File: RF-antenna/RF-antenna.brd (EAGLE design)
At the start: 108.2 x 108.2 mm, 48 parts, among them CON1 UMC_CONNECTORREGULAR, CON2 UMC_CONNECTORREGULAR, CON3 UMC_CONNECTORREGULAR, CON4 UMC_CONNECTORREGULAR, CON5 UMC_CONNECTORREGULAR, CON6 UMC_CONNECTORREGULAR, U1 THS3091DDAR, U2 THS3091DDAR, U3 THS3091DDAR

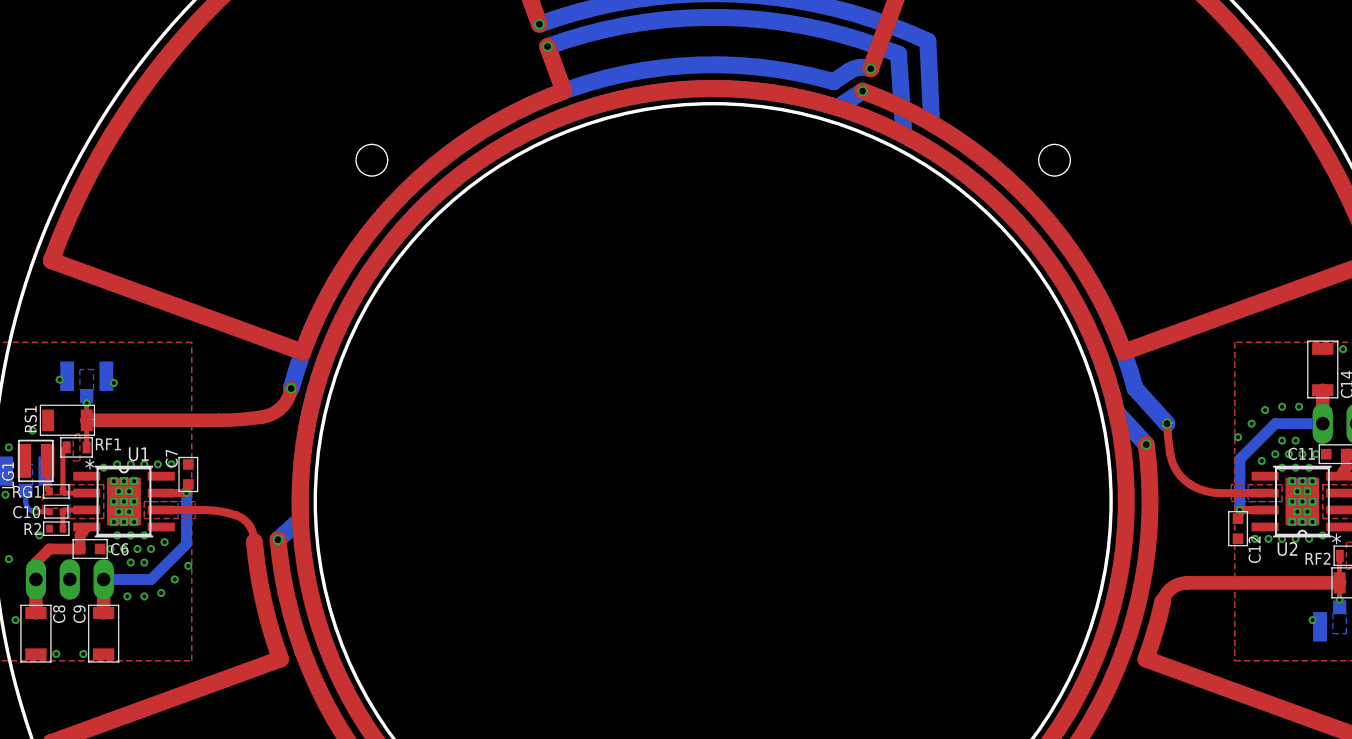
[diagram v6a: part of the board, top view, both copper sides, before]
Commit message: Fix antenna polarity
The polarity of half of each of the D-shaped antennas was incorrect. I've adjusted so that the D antennas produce B fields pointing along the diagonal as desired.

DSB
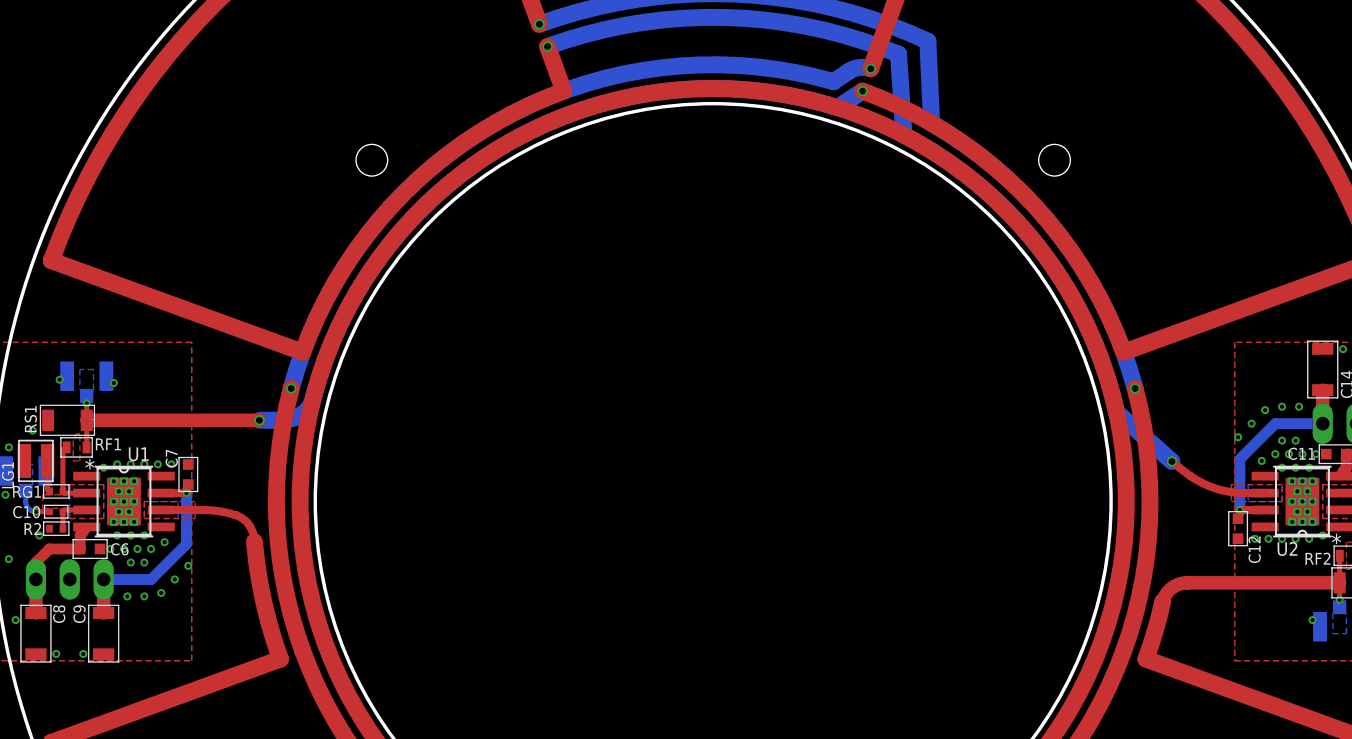
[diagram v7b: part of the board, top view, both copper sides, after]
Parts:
- moved LW5 8.95 mm to (95.5, 54.8)
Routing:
- net D1_COIL: track 372.8 -> 377.4 mm
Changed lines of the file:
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@@
 <element name="LW3" library="RFantenna" package="LITZ_100MHZ" value="LITZ_TERM" x="19.685" y="51.1048"/>
 <element name="LW4" library="RFantenna" package="LITZ_100MHZ" value="LITZ_TERM" x="7.112" y="60.198"/>
-<element name="LW5" library="RFantenna" package="LITZ_100MHZ" value="LITZ_TERM" x="88.138" y="59.944"/>
+<element name="LW5" library="RFantenna" package="LITZ_100MHZ" value="LITZ_TERM" x="95.4532" y="54.7878"/>
 <element name="LW6" library="RFantenna" package="LITZ_100MHZ" value="LITZ_TERM" x="101.092" y="48.006"/>
 </elements>
@@
 <wire x1="53.34" y1="21.9456" x2="52.324" y2="23.114" width="1.016" layer="1" curve="72.387043"/>
 <wire x1="55.88" y1="23.114" x2="55.858796875" y2="23.1638375" width="0" layer="19" extent="1-1"/>
-<wire x1="52.324" y1="23.114" x2="52.345203125" y2="23.1638375" width="0" layer="19" extent="1-1"/>
+<wire x1="52.345203125" y1="23.1638375" x2="52.324" y2="23.114" width="0" layer="19" extent="1-1"/>
 </signal>
 <signal name="D1_COIL">
@@
 <wire x1="4.456159375" y1="36.032390625" x2="21.641259375" y2="42.28725625" width="1.27" layer="1"/>
 <wire x1="21.641259375" y1="42.28725625" x2="19.689453125" y2="51.091290625" width="1.27" layer="1" curve="-14.999998"/>
-<wire x1="23.31203125" y1="42.89536875" x2="21.460684375" y2="51.24625625" width="1.27" layer="1" curve="-15.000001"/>
 <wire x1="103.747840625" y1="72.171609375" x2="72.171609375" y2="103.747840625" width="1.27" layer="1" curve="49.999998"/>
 <wire x1="84.89196875" y1="65.30863125" x2="65.30863125" y2="84.89196875" width="1.27" layer="1" curve="50.000003"/>
 <wire x1="84.89196875" y1="65.30863125" x2="103.747840625" y2="72.171609375" width="1.27" layer="1"/>
-<via x="21.460684375" y="51.24625625" extent="1-16" drill="0.508"/>
 <via x="65.30863125" y="84.89196875" extent="1-16" drill="0.508"/>
 <wire x1="72.171609375" y1="103.747840625" x2="65.91674375" y2="86.562740625" width="1.27" layer="1"/>
 <wire x1="63.133534375" y1="85.5987" x2="22.452475" y2="62.582465625" width="1.27" layer="16" curve="91"/>
-<wire x1="63.420271875" y1="83.65578125" x2="23.14349375" y2="52.750321875" width="1.27" layer="16" curve="110.000002"/>
 <wire x1="63.420271875" y1="83.65578125" x2="65.30863125" y2="84.89196875" width="1.27" layer="16"/>
 <wire x1="63.133534375" y1="85.5987" x2="64.262" y2="86.36" width="1.27" layer="16"/>
 <wire x1="64.262" y1="86.36" x2="65.91674375" y2="86.562740625" width="1.27" layer="16" curve="-54.03957"/>
 <via x="65.91674375" y="86.562740625" extent="1-16" drill="0.508"/>
-<wire x1="23.14349375" y1="52.750321875" x2="21.460684375" y2="51.24625625" width="1.27" layer="16"/>
 <wire x1="12.7" y1="53.467" x2="15.8496" y2="53.467" width="0.6096" layer="1"/>
 <wire x1="15.8496" y1="53.467" x2="18.288" y2="53.086" width="0.6096" layer="1" curve="-17.761316"/>
@@
 <wire x1="19.304" y1="52.324" x2="19.685" y2="51.1048" width="0.6096" layer="1" curve="-33.335057"/>
 <via x="22.452475" y="62.582465625" extent="1-16" drill="0.508"/>
-<wire x1="7.1142" y1="60.198" x2="17.018" y2="60.198" width="1.016" layer="1"/>
-<wire x1="17.018" y1="60.198" x2="20.32" y2="60.452" width="1.016" layer="1" curve="8.797411"/>
-<wire x1="20.32" y1="60.452" x2="22.452475" y2="62.582465625" width="1.016" layer="1" curve="72.351251"/>
+<wire x1="23.31203125" y1="42.89536875" x2="22.452475" y2="62.582465625" width="1.27" layer="1" curve="-35"/>
+<wire x1="63.420271875" y1="83.65578125" x2="24.169890625" y2="62.122284375" width="1.27" layer="16" curve="92.500001"/>
+<wire x1="24.169890625" y1="62.122284375" x2="24.0538" y2="61.6458" width="1.27" layer="16"/>
+<wire x1="24.0538" y1="61.6458" x2="22.9108" y2="60.452" width="1.27" layer="16" curve="-44.249514"/>
+<wire x1="22.9108" y1="60.452" x2="21.1582" y2="60.198" width="1.27" layer="16" curve="-24.404178"/>
+<wire x1="21.1582" y1="60.198" x2="20.066" y2="60.198" width="1.27" layer="16"/>
+<via x="20.066" y="60.198" extent="1-16" drill="0.508"/>
+<wire x1="7.1142" y1="60.198" x2="20.066" y2="60.198" width="1.016" layer="1"/>
 <wire x1="19.689453125" y1="51.091290625" x2="19.685" y2="51.1048" width="0" layer="19" extent="1-1"/>
 <wire x1="7.112" y1="60.198" x2="7.112" y2="60.2002" width="0" layer="19" extent="1-1"/>
@@
 <wire x1="103.747840625" y1="36.032390625" x2="86.562740625" y2="42.28725625" width="1.27" layer="1"/>
 <wire x1="86.562740625" y1="42.28725625" x2="87.82716875" y2="46.625309375" width="1.27" layer="1" curve="7.499999"/>
-<wire x1="84.89196875" y1="42.89536875" x2="86.58768125" y2="58.378821875" width="1.27" layer="1" curve="27.5"/>
 <wire x1="68.410665625" y1="81.588690625" x2="84.355459375" y2="60.80903125" width="1.27" layer="16" curve="-49.999998"/>
 <wire x1="70.485" y1="82.4781875" x2="85.751525" y2="62.582465625" width="1.27" layer="16" curve="-44.999998"/>
 <wire x1="70.485" y1="82.4781875" x2="70.20375625" y2="88.632325" width="1.27" layer="16"/>
 <wire x1="68.410665625" y1="81.588690625" x2="68.001828125" y2="87.659153125" width="1.27" layer="16"/>
-<wire x1="84.355459375" y1="60.80903125" x2="86.58768125" y2="58.378821875" width="1.27" layer="16"/>
-<via x="86.58768125" y="58.378821875" extent="1-16" drill="0.508"/>
-<wire x1="85.751525" y1="62.582465625" x2="88.138" y2="59.944" width="1.27" layer="16"/>
-<via x="88.138" y="59.944" extent="1-16" drill="0.508"/>
 <wire x1="89.662" y1="48.006" x2="87.82716875" y2="46.625309375" width="1.016" layer="1" curve="73.92207"/>
 <wire x1="101.0898" y1="48.006" x2="89.662" y2="48.006" width="1.016" layer="1"/>
-<wire x1="95.504" y1="54.737" x2="92.1512" y2="54.737" width="0.6096" layer="1"/>
-<wire x1="92.1512" y1="54.737" x2="89.916" y2="55.372" width="0.6096" layer="1" curve="-31.718725"/>
-<wire x1="89.916" y1="55.372" x2="88.392" y2="57.658" width="0.6096" layer="1" curve="-49.182377"/>
-<wire x1="88.392" y1="57.658" x2="88.138" y2="59.944" width="0.6096" layer="1" curve="-5.517365"/>
-<wire x1="101.092" y1="48.0038" x2="101.092" y2="48.006" width="0" layer="19" extent="1-1"/>
+<wire x1="84.89196875" y1="42.89536875" x2="85.751525" y2="62.582465625" width="1.27" layer="1" curve="35"/>
+<via x="85.751525" y="62.582465625" extent="1-16" drill="0.508"/>
+<wire x1="84.355459375" y1="60.80903125" x2="88.51455" y2="57.112709375" width="1.27" layer="16"/>
+<wire x1="95.504" y1="54.737" x2="93.98" y2="54.737" width="0.6096" layer="1"/>
+<wire x1="93.98" y1="54.737" x2="89.916" y2="56.007" width="0.6096" layer="1" curve="-34.708049"/>
+<wire x1="89.916" y1="56.007" x2="88.51455" y2="57.112709375" width="0.6096" layer="1" curve="-7.129041"/>
+<via x="88.51455" y="57.112709375" extent="1-16" drill="0.508"/>
+<wire x1="95.504" y1="54.737" x2="95.4532" y2="54.7878" width="0" layer="19" extent="1-1"/>
+<wire x1="101.092" y1="48.006" x2="101.092" y2="48.0038" width="0" layer="19" extent="1-1"/>
 </signal>
 </signals>

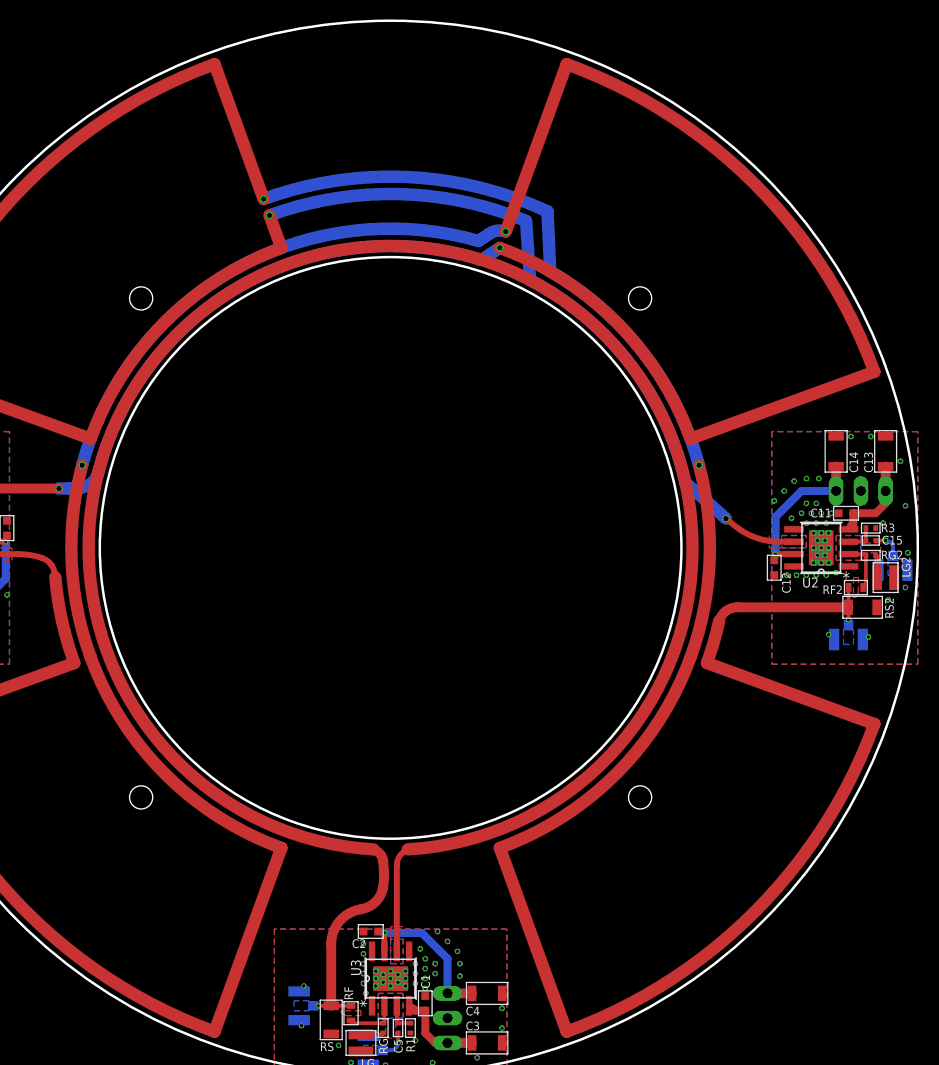
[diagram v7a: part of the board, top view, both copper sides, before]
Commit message: Test board ready
Pushing the prepared test board complete with 230 MHz and 6.8 GHz antennas for hyperfine control.

DSB
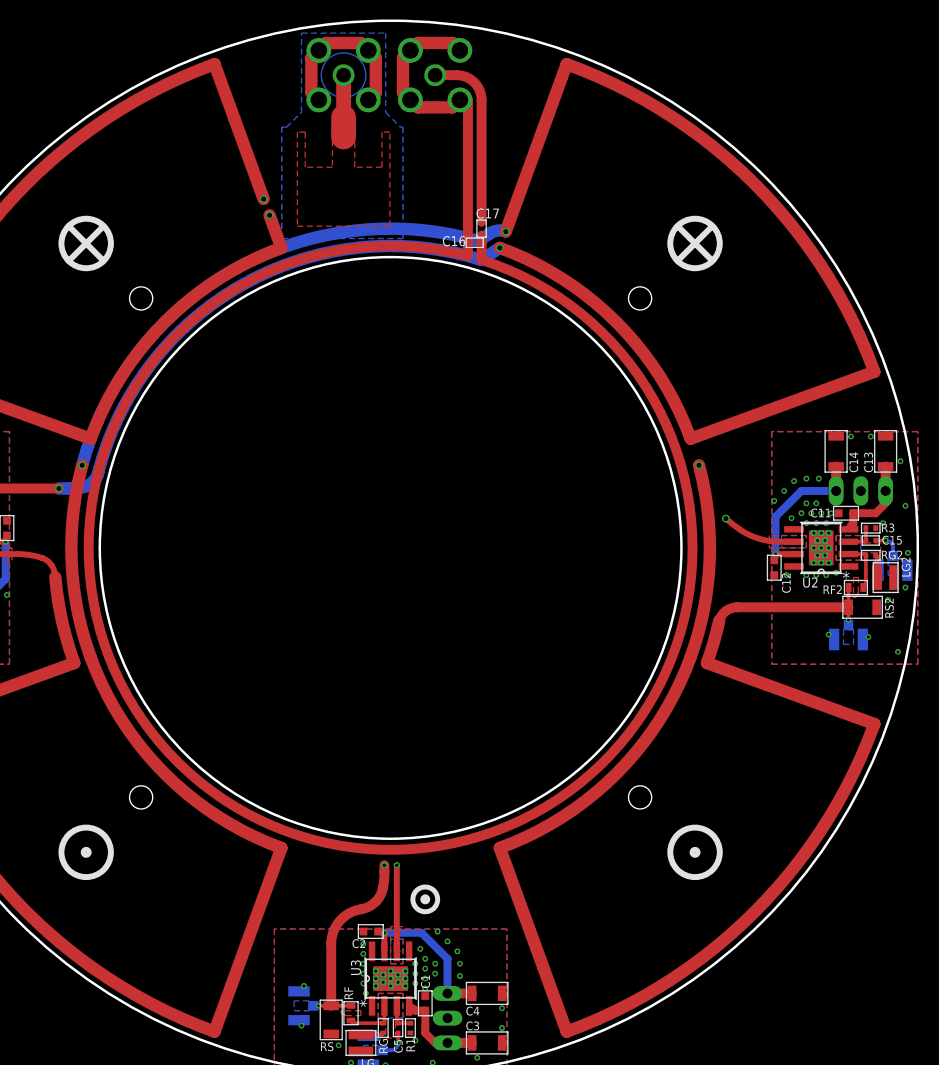
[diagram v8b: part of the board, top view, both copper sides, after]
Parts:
- added C16: 3pF, jqi_passives:C_MLCC_0402
- added C17: 0.3pF, jqi_passives:C_MLCC_0402
- added X1, X2: SMA-V, connector-jqi:SMA-V
- moved LW2 16.6 mm to (48.0, 7.11)
- moved LW1 10.5 mm to (54.7, 12.7)
- moved LW5 0.07 mm to (95.5, 54.7)
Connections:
- new net COIL6LI_N: C16.P$1, C16.P$2, C17.P$2, X2.GND1, X2.GND2, X2.GND3, X2.GND4
- new net COIL6LI_P: C17.P$1, X2.RF
- new net COIL87RB_GND: X1.GND1, X1.GND2, X1.GND3, X1.GND4
- new net COIL87RB_IN: X1.RF
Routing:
- net COIL6LI_N: track 0.00 -> 41.3 mm
- net COIL6LI_P: track 0.00 -> 18.5 mm
- net COIL87RB_GND: track 0.00 -> 17.1 mm
- net COIL87RB_IN: track 0.00 -> 6.35 mm
- net R_COIL: track 37.1 -> 37.2 mm, vias 1 -> 3
- added copper zone on layer 16, net COIL87RB_GND
- added copper zone on layer 1, net COIL87RB_IN
